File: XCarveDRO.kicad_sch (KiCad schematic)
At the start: 6 parts, among them J103 USB_A, SW103 SEL1, SW104 SEL2, U101 Teensy4.1

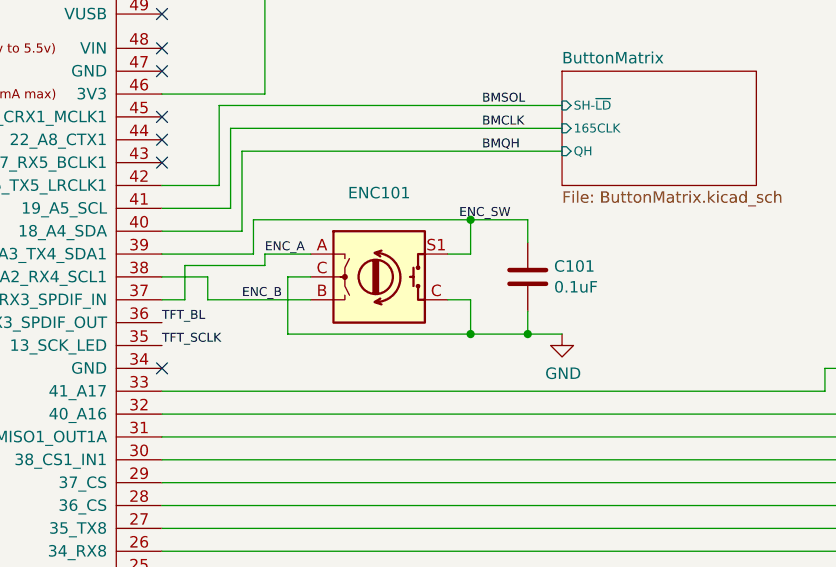
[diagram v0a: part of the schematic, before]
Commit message: Move encoder into its own sheet. Replace with MPG/Encoder combo.
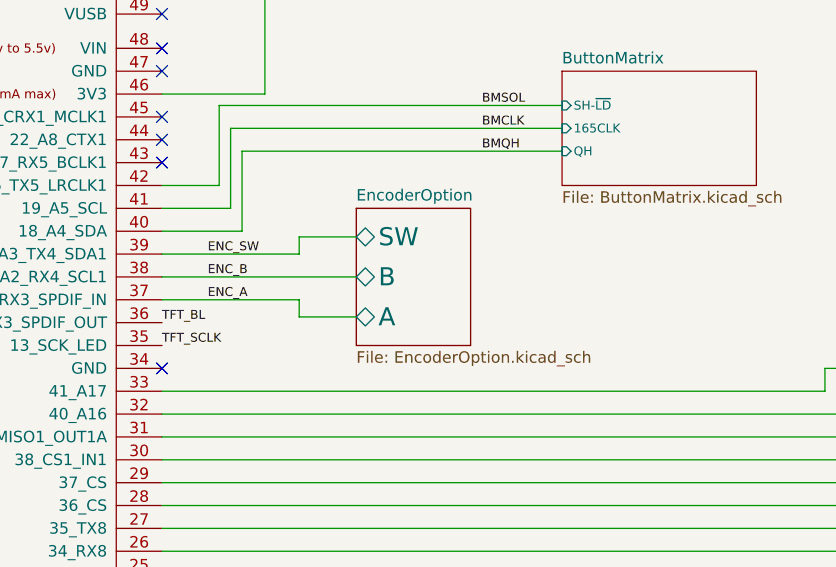
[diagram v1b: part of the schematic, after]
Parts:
- removed C101: 0.1uF, symbol Device:C
- removed ENC101: Encoder, MarcoK:TSWA3NCD23LFS-NavScroll-Switch, symbol MarcoK:TSWA3NCD23LFS-NavScroll-Switch
- SW103, SW104: footprint Marco:SWITCH_ROTARY_4-12 -> MarcoK:SWITCH_ROTARY_4-12
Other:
- added sheet EncoderOption (EncoderOption.kicad_sch)

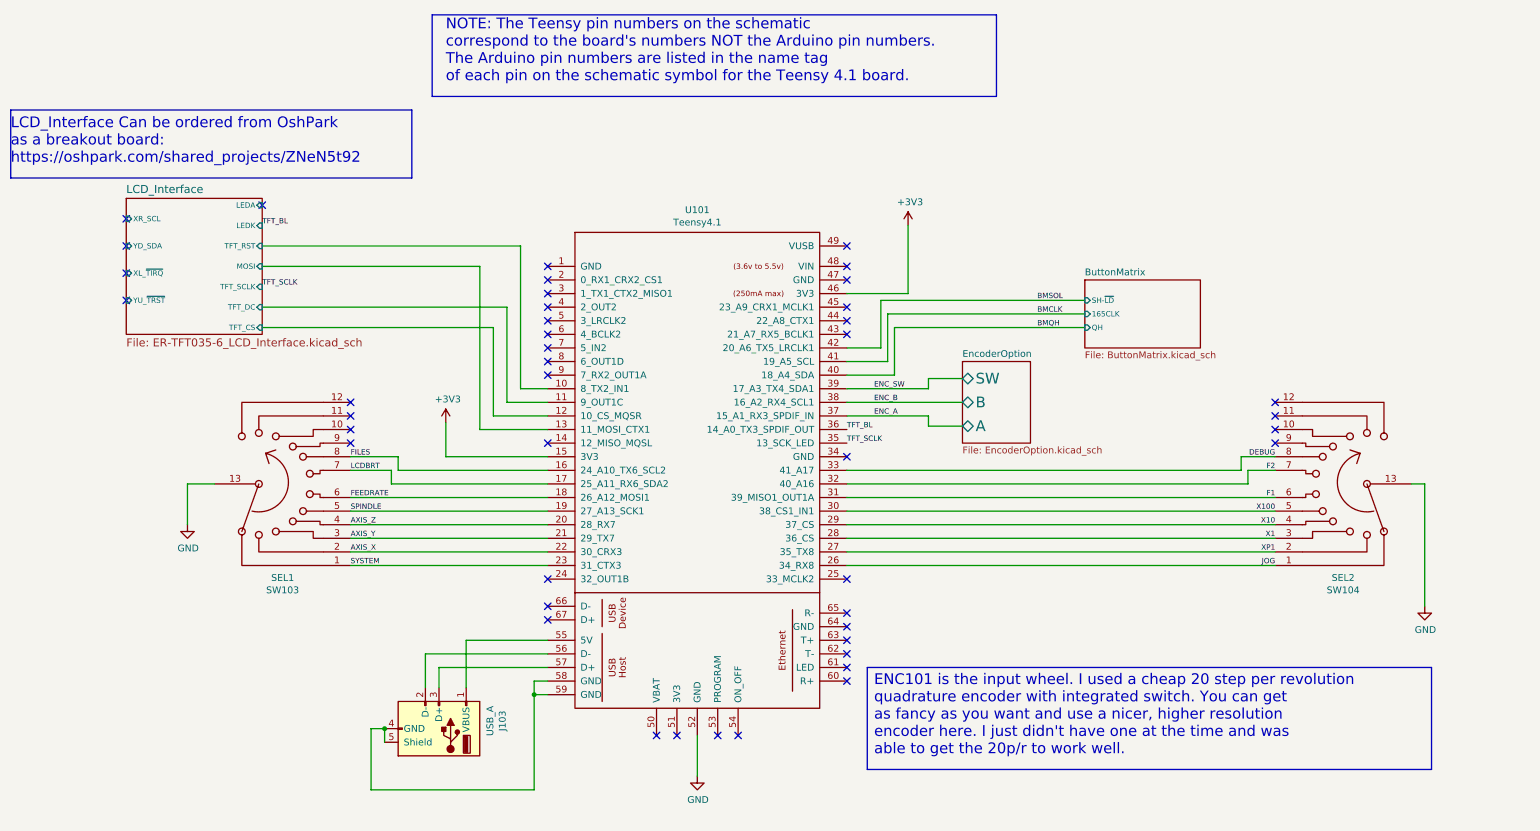
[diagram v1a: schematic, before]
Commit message: Added the MPG. Switched tactile button model. Added JLC design rules.
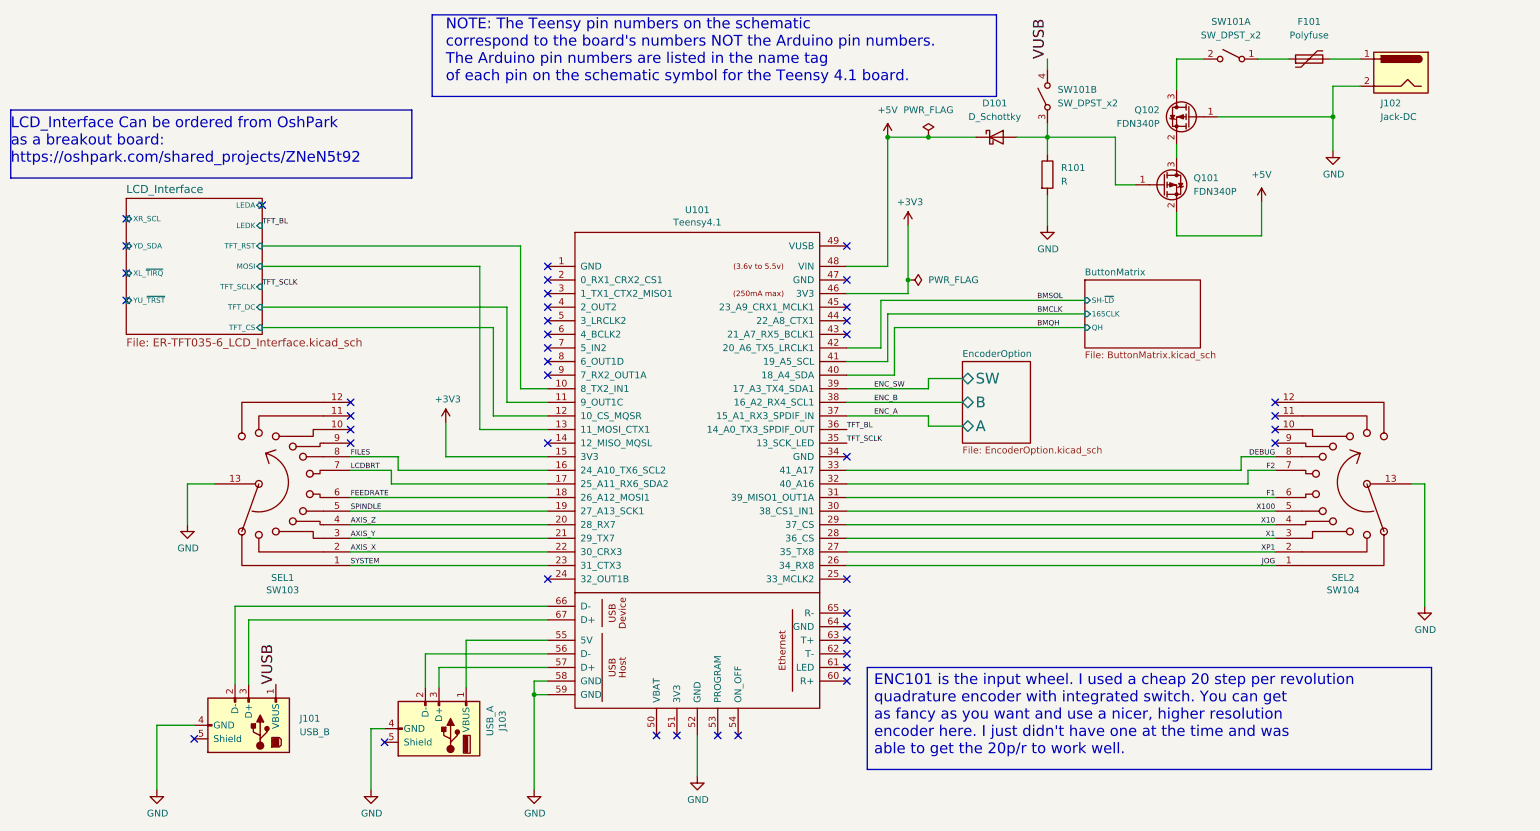
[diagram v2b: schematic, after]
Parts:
- added D101: D_Schottky, Diode_SMD:D_SOD-323_HandSoldering, symbol Device:D_Schottky
- added F101: Polyfuse, Fuse:Fuse_1210_3225Metric_Pad1.42x2.65mm_HandSolder, symbol Device:Polyfuse
- added J101: USB_B, Connector_USB:USB_B_Lumberg_2411_02_Horizontal, symbol Connector:USB_B
- added J102: Jack-DC, Connector_PinHeader_2.54mm:PinHeader_1x02_P2.54mm_Vertical, symbol Connector:Jack-DC
- added Q101, Q102: FDN340P, Package_TO_SOT_SMD:SOT-23, symbol Transistor_FET:FDN340P
- added R101: R, Resistor_SMD:R_0805_2012Metric_Pad1.20x1.40mm_HandSolder, symbol Device:R
- added SW101: SW_DPST_x2, Connector_PinHeader_2.54mm:PinHeader_1x04_P2.54mm_Vertical, symbol Switch:SW_DPST_x2
- SW103, SW104: footprint MarcoK:SWITCH_ROTARY_4-12 -> MarcoK:SWITCH_ROTARY_4-12-No_Cuts
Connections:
- net GND: now also J103.4 (GND), U101.58 (GND), U101.59 (GND), J101.4 (GND), J102.2, Q102.1 (G), R101.2
- net +5V: now reaches U101.48 (VIN)
- net +5V: now also D101.1 (K), Q101.2 (S)
- net at U101.66 (D-): now also J101.2 (D-)
- net at U101.67 (D+): now also J101.3 (D+)
- new net: Q101.3 (D), Q102.2 (S)
- new net: Q102.3 (D), SW101.2 (B)
- new net: D101.2 (A), Q101.1 (G), R101.1, SW101.3 (A)
- new net: F101.2, J102.1
- new net: F101.1, SW101.1 (A)
- new net VUSB: J101.1 (VBUS), SW101.4 (B)
- now unconnected: J103.5 (Shield)
- no-connect marks 44 -> 43
